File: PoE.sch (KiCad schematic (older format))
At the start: 25 parts, among them IC1 TPS2378DDA

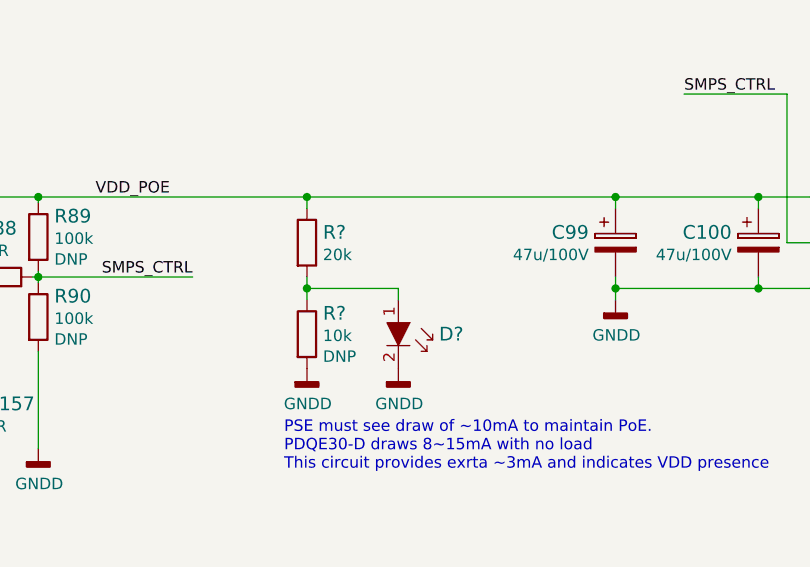
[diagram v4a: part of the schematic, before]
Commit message: Annotate parts
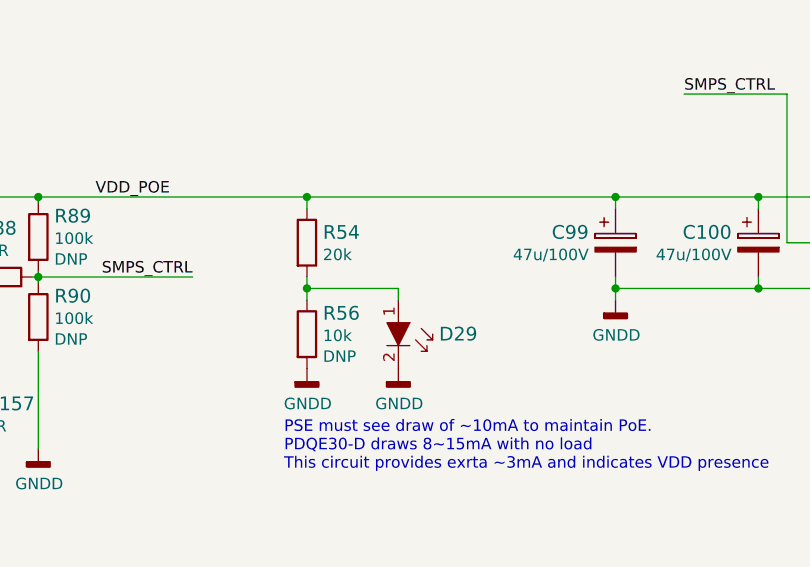
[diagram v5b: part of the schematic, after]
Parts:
- gave numbers to parts that had none: 3
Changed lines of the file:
@@
 	11975 5025 12625 5025
 $Comp
-L sa800u-baseboard-hw:R_20k_0603 R?
+L sa800u-baseboard-hw:R_20k_0603 R54
 U 1 1 62C10670
 P 8575 4825
-F 0 "R?" V 8530 4895 60  0000 L CNN
+F 0 "R54" V 8530 4895 60  0000 L CNN
 F 1 "R_20k_0603" H 8575 4675 60  0001 C CNN
 F 2 "sa800u-baseboard-hw-footprints:0603-res" H 8775 5025 60  0001 L CNN
@@
 	8575 4975 8575 5025
 $Comp
-L sa800u-baseboard-hw:R_10k_0603 R?
+L sa800u-baseboard-hw:R_10k_0603 R56
 U 1 1 62C1B70F
 P 8575 5225
-F 0 "R?" V 8484 5295 60  0000 L CNN
+F 0 "R56" V 8484 5295 60  0000 L CNN
 F 1 "R_10k_0603" H 8575 5075 60  0001 C CNN
 F 2 "sa800u-baseboard-hw-footprints:0603-res" H 8775 5425 60  0001 L CNN
@@
 $EndComp
 $Comp
-L sa800u-baseboard-hw:GNDD #PWR?
+L sa800u-baseboard-hw:GNDD #PWR0254
 U 1 1 62C1C906
 P 8575 5375
-F 0 "#PWR?" H 8575 5125 50  0001 C CNN
+F 0 "#PWR0254" H 8575 5125 50  0001 C CNN
 F 1 "GNDD" H 8579 5220 50  0000 C CNN
 F 2 "" H 8575 5375 50  0001 C CNN
@@
 	8575 5025 8575 5075
 $Comp
-L sa800u-baseboard-hw:KP-1608EC D?
+L sa800u-baseboard-hw:KP-1608EC D29
 U 1 1 62C25BE8
 P 8975 5275
-F 0 "D?" V 8925 5453 60  0000 L CNN
+F 0 "D29" V 8925 5453 60  0000 L CNN
 F 1 "KP-1608EC" V 8978 5453 60  0001 L CNN
 F 2 "sa800u-baseboard-hw-footprints:LED_0603" H 9175 5475 60  0001 L CNN
@@
 $EndComp
 $Comp
-L sa800u-baseboard-hw:GNDD #PWR?
+L sa800u-baseboard-hw:GNDD #PWR0255
 U 1 1 62C271AD
 P 8975 5375
-F 0 "#PWR?" H 8975 5125 50  0001 C CNN
+F 0 "#PWR0255" H 8975 5125 50  0001 C CNN
 F 1 "GNDD" H 8979 5220 50  0000 C CNN
 F 2 "" H 8975 5375 50  0001 C CNN
